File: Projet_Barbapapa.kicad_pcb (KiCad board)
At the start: 4 copper layers, 88.1 x 106.6 mm, 33 parts, among them J1 USB_C_Receptacle_USB2.0, J2 Speaker, J3 Conn_01x02, J4 LCD SPI, J5 LCD Soft SPI, J6 Random FTDI, J7 NFC1, J8 NFC2, J9 RGB_LED, SW1 SW_DPST, U1 MAX98357A/B, U2 AP61201Z6-7 buck, U3 MAX1811, U4 CD4051B

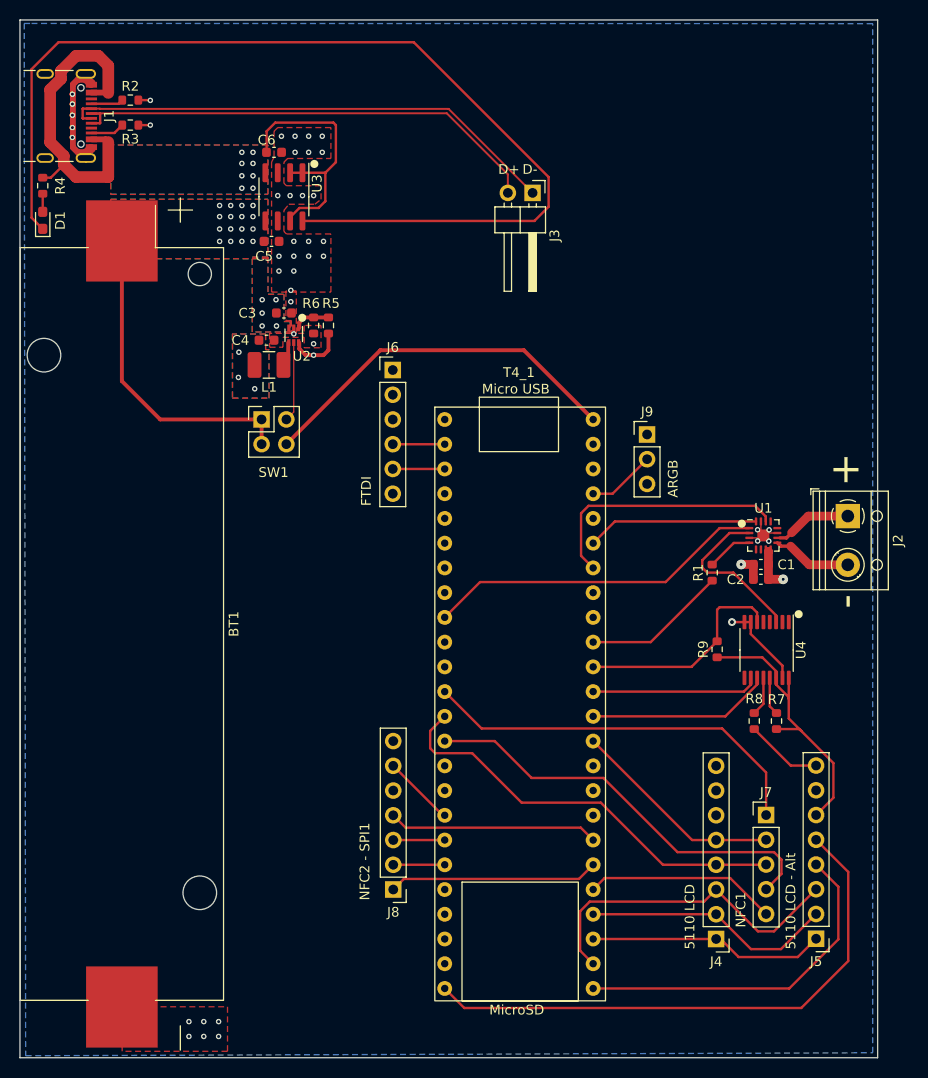
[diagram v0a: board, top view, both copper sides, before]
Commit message: Améliorations après retour Victor
Allumage du régulateur maintenant géré par la teensy
Compaction de la carte pour rentrer sur 100x100mm
Ajout des trous de montage
Routage de la puissance du port USB maintenant sans boucle !
Un peu plus d'espace pour l'ampli'
Routage de l'ampli' avec des plans sur la sortie et une via par
condo pour l'entrée.
Moins de vias thermiques
Un seule via dans le pad de l'ampli'
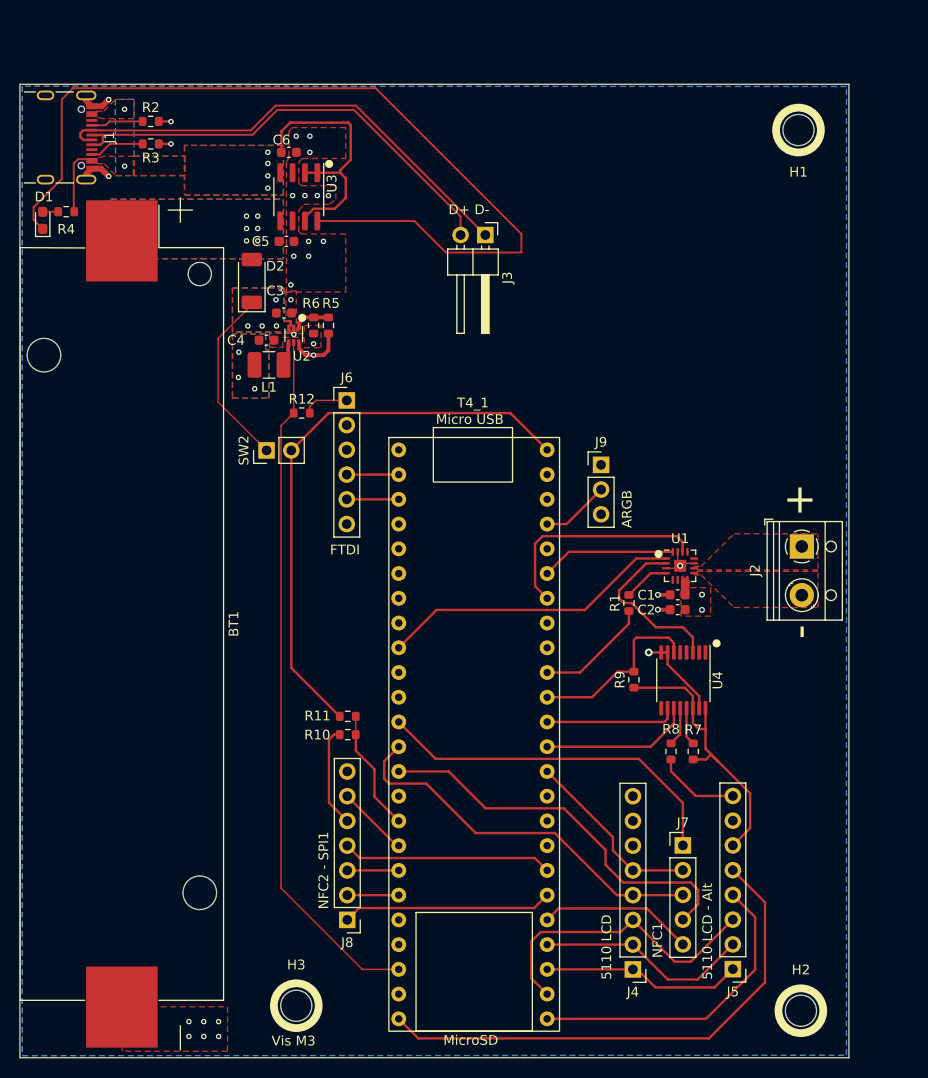
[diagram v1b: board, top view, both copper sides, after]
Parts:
- removed SW1: SW_DPST, Connector_PinHeader_2.54mm:PinHeader_2x02_P2.54mm_Vertical
- added D2: PMEG3050EP-QX, Diode_SMD:D_SOD-128, F.Cu at (41.4, 82.3)
- added H1: MountingHole, MountingHole:MountingHole_3.2mm_M3, F.Cu at (97.5, 66.8)
- added H2: MountingHole, MountingHole:MountingHole_3.2mm_M3, F.Cu at (97.8, 157.2)
- added H3: MountingHole, MountingHole:MountingHole_3.2mm_M3, F.Cu at (46.0, 156.7)
- added R10: RES_0603_200k_1%, 01_Passives:RES_0603, F.Cu at (51.3, 128.9)
- added R11: RES_0603_100K_1%, 01_Passives:RES_0603, F.Cu at (51.3, 127.0)
- added R12: RES_0603_5K1_1%, 01_Passives:RES_0603, F.Cu at (46.5, 95.9)
- added SW2: Power switch, Connector_PinHeader_2.54mm:PinHeader_1x02_P2.54mm_Vertical, F.Cu at (42.9, 99.7)
- R9: value RES_0603_2K1_1% -> RES_0603_5K1_1%
- moved J4 9.10 mm to (80.5, 153.0)
- moved C1 9.10 mm to (85.1, 114.5)
- moved C2 9.10 mm to (85.1, 116.0)
- moved J5 9.10 mm to (90.8, 153.0)
- moved J7 9.10 mm to (85.7, 140.3)
- moved R1 9.10 mm to (80.1, 115.4)
- moved R9 9.10 mm to (80.6, 123.2)
- moved U1 9.10 mm to (85.4, 111.5)
- moved U4 9.10 mm to (85.7, 123.3)
- moved R7 9.10 mm to (86.7, 130.6)
- moved R8 9.10 mm to (84.4, 130.6)
- moved J3 6.50 mm to (65.4, 77.6)
- moved J9 5.66 mm to (77.3, 101.2)
- moved J6 5.66 mm to (51.2, 94.6)
- moved J2 5.66 mm to (97.9, 109.6)
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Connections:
- C3 pad 1: /Power and USB/BATT_LOAD -> /Power and USB/BATT_SAFE
- T4_1 pad 24: unconnected-(T4_1-A10-Pad24) -> /BAT_SNS
- T4_1 pad 30: unconnected-(T4_1-Pad30) -> /Reg_en
- U2 pad 3: /Power and USB/BATT_LOAD -> /Power and USB/BATT_SAFE
- U2 pad 5: /Power and USB/Reg_en -> /Reg_en
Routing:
- net /Reg_en: track 0.00 -> 72.1 mm
- net /Power and USB/BATT_LOAD: track 32.9 -> 0.00 mm, vias 21 -> 6
- net /Power and USB/VBUS: track 60.7 -> 34.0 mm, vias 8 -> 6
- net /Power and USB/VIN: track 38.4 -> 58.8 mm
- net /Power and USB/BATT_SAFE: track 0.00 -> 18.8 mm, vias 0 -> 4
- net Net-(D1-K): track 105.8 -> 93.0 mm
- net /BAT_SNS: track 0.00 -> 12.6 mm
- net /Power and USB/Reg_en: track 8.21 -> 0.00 mm
- net /Audio/Speaker_N: track 8.17 -> 0.00 mm
- net /Audio/Speaker_P: track 7.88 -> 0.00 mm
- net /LCD connectors/LCD_SCK_ALT: track 58.1 -> 53.7 mm
- net /LCD connectors/LCD_RST: track 24.4 -> 20.2 mm
- net /LCD connectors/LCD_CS: track 25.9 -> 22.0 mm
- net /Audio_OUT: track 35.1 -> 31.2 mm
- net /NFC1_RST: track 19.8 -> 15.9 mm
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- added copper zone on F.Cu, net /Audio/Speaker_N
- added copper zone on F.Cu, net /Audio/Speaker_P
- added copper zone on B.Cu, net /Power and USB/BATT_SAFE
- added copper zone on F.Cu, net /Power and USB/BATT_SAFE
- added copper zone on In2.Cu, net /Power and USB/BATT_SAFE
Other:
- board size 88.1 x 106.6 mm -> 85.1 x 99.9 mm
- board text added: "L1 to the right One hop this time Bouger les résistances"
- board text added: "Vis M3"
- board text removed: "Pour dissipation thermique : ils disent de mettre des vias dans le pad, comment ?"
- board text removed: "The fuck do I do for thermal dissipation ? Ça dit de mettre des vias, mais pas de specs de dimension/nombre..."

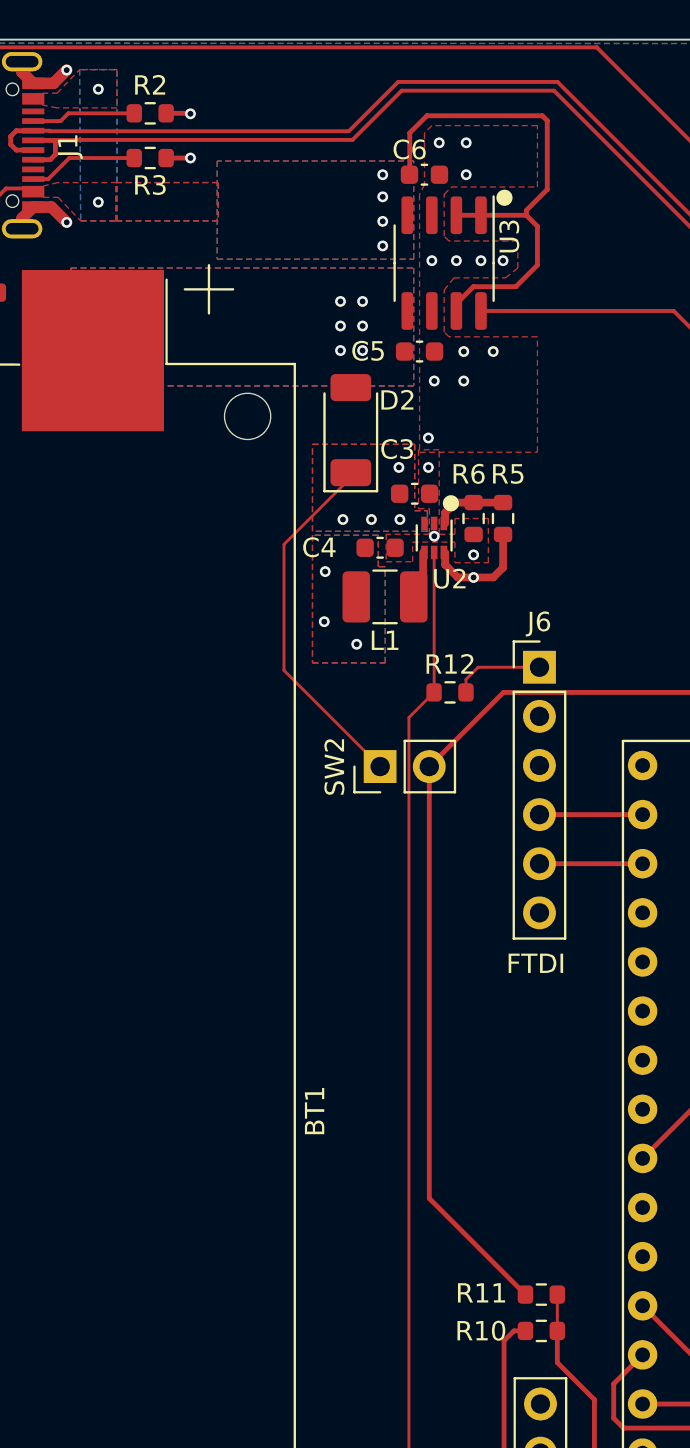
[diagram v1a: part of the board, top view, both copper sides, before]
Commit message: Inversion de la bobine de régulateur
180° à la bobine du régulateur pour faciliter le routage et le placement
Plus d'espace autour du régulateur.
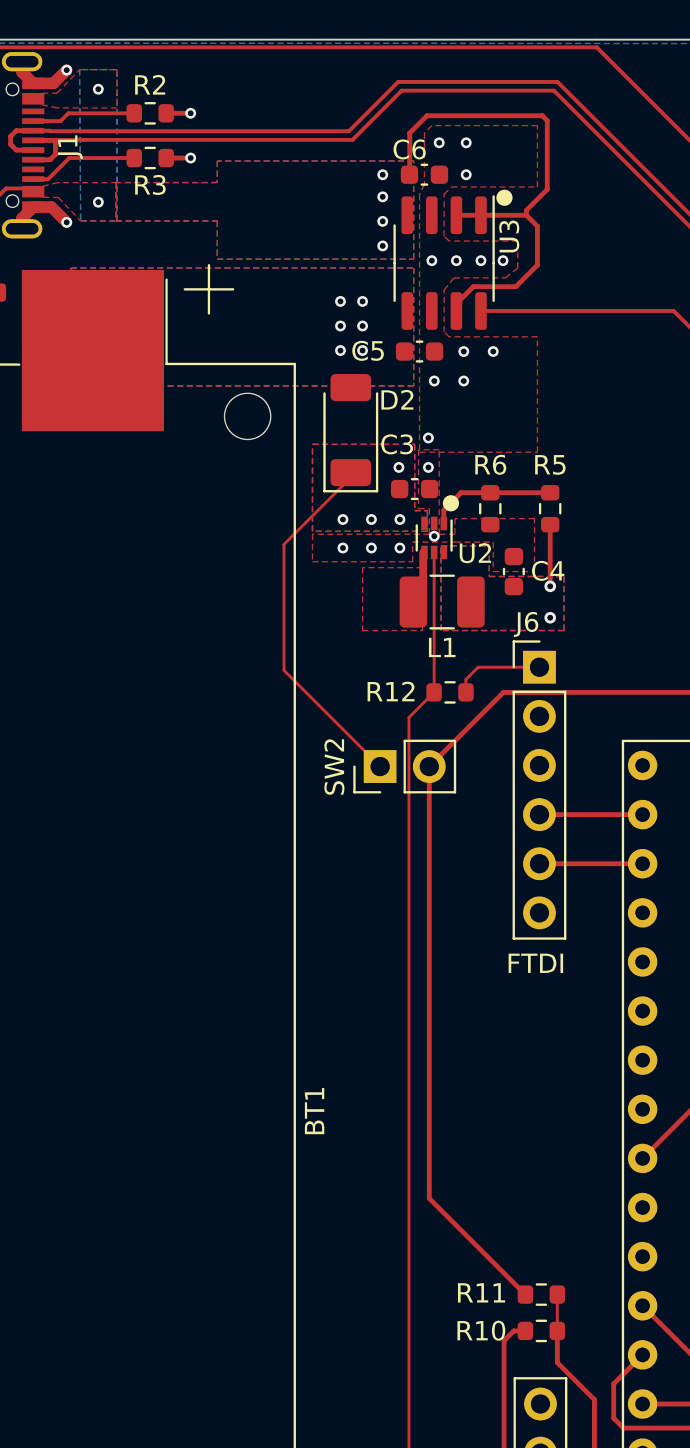
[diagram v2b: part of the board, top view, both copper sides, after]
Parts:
- moved C4 7.03 mm to (49.8, 89.6), turned to -90 degrees
- moved L1 2.97 mm to (46.1, 91.2), turned to 0 degrees
- moved R5 2.49 mm to (51.7, 86.4)
- moved R6 1.00 mm to (48.6, 86.4)
- moved C3 0.24 mm to (44.7, 85.3)
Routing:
- net Net-(U2-FB): track 3.77 -> 6.57 mm
- net /+3.3V: track 37.7 -> 35.0 mm, vias 6 -> 4
- net Net-(U2-SW): track 2.50 -> 1.82 mm
- net VSS: track 48.3 -> 48.2 mm, vias 29 -> 31
- added copper zone on F.Cu, net Net-(U2-SW)
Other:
- board text removed: "L1 to the right One hop this time Bouger les résistances"

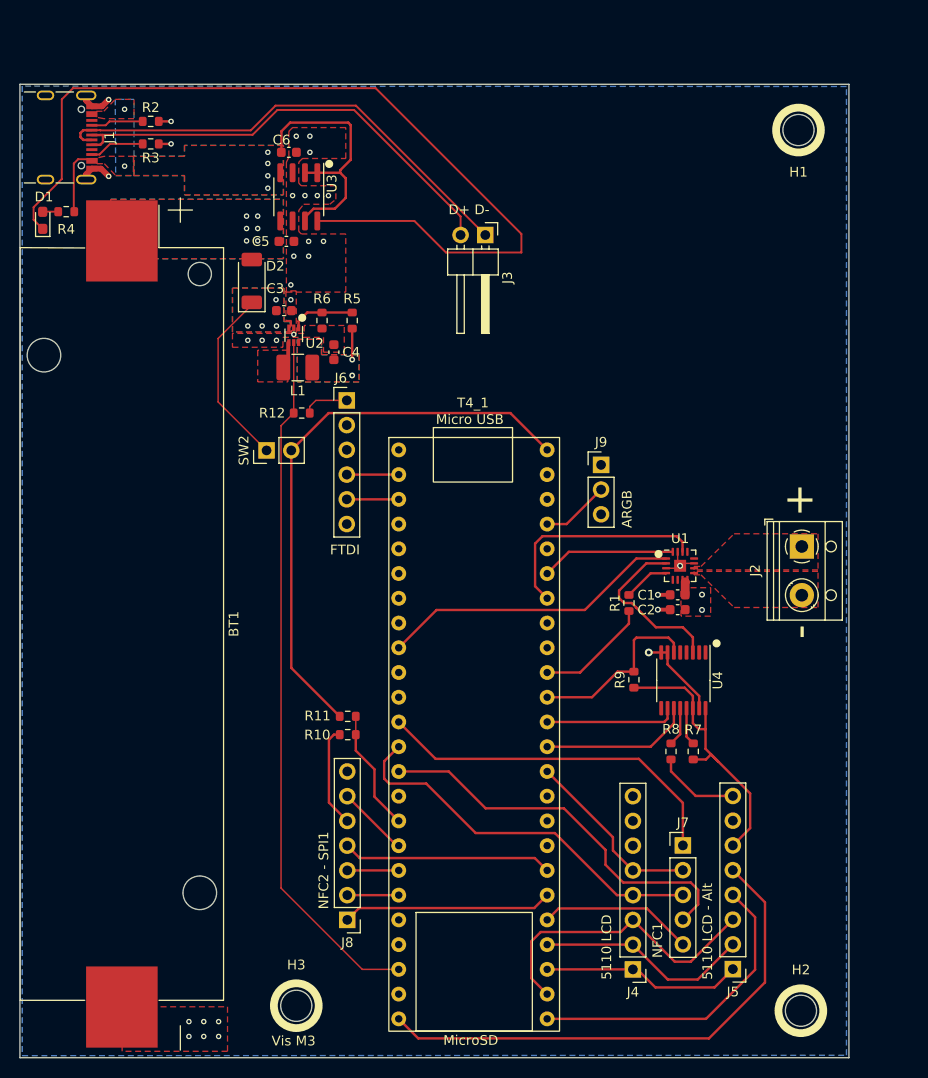
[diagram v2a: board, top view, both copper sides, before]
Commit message: Rev 0.3: Passage sur deux couches
Passage sur deux couches, ajustement de l'impédance pour l'USB.
Reroutage de l'alimentation côté USB
Ajout de beaucoup de silk
Quelques ajustements de nets pour la lisbilité
Ajout de LEDs de debug
Plan de masse sur le top
Quelques mises à jour sur le schematic
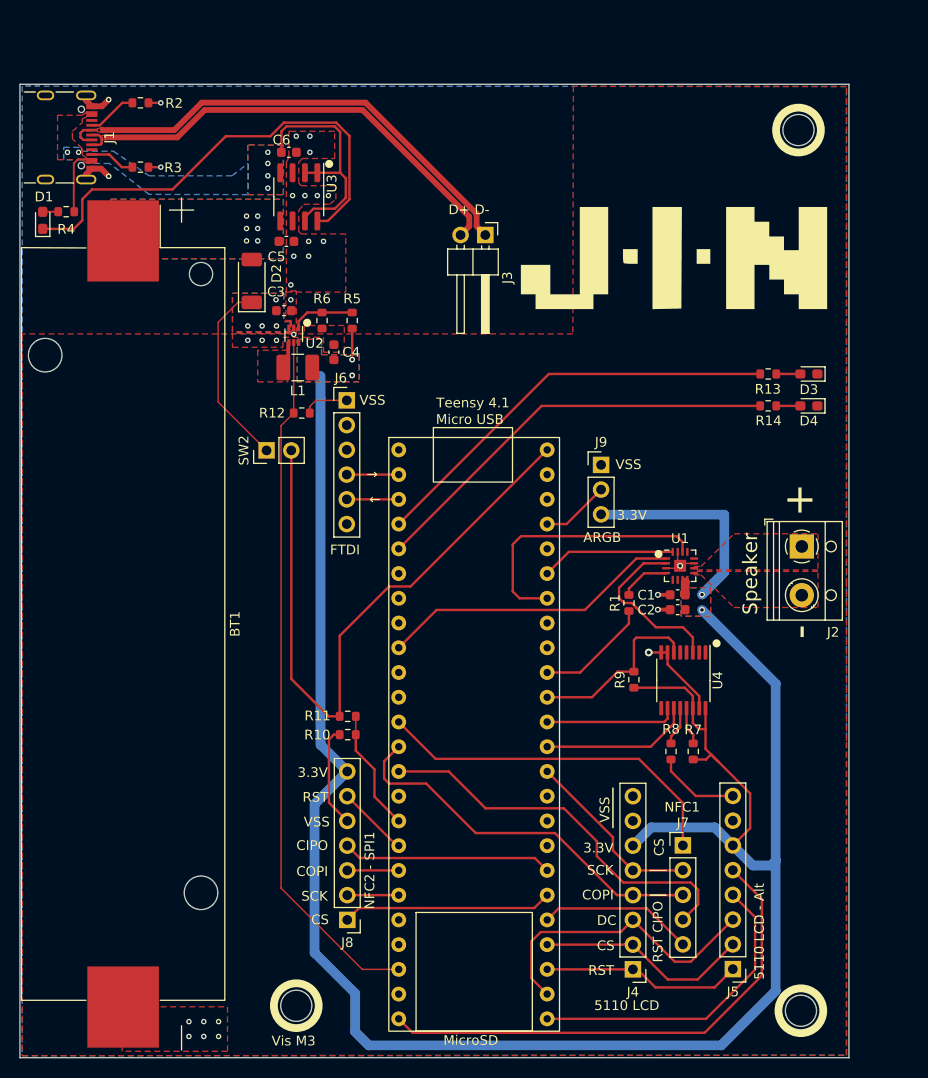
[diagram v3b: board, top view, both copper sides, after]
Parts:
- added D3: LED, LED_SMD:LED_0603_1608Metric_Pad1.05x0.95mm_HandSolder, F.Cu at (98.6, 91.8)
- added D4: LED, LED_SMD:LED_0603_1608Metric_Pad1.05x0.95mm_HandSolder, F.Cu at (98.6, 95.1)
- added G***: LOGO, LOGO, F.Cu at (85.2, 80.2)
- added G***: LOGO, LOGO, F.Cu at (80.9, 86.6)
- added R13: RES_0603_200_1%, 01_Passives:RES_0603, F.Cu at (94.4, 91.8)
- added R14: RES_0603_200_1%, 01_Passives:RES_0603, F.Cu at (94.4, 95.1)
- added REF**: OSHW-Logo2_14.6x12mm_SilkScreen, Symbol:OSHW-Logo2_14.6x12mm_SilkScreen, B.Cu at (28.0, 88.2)
- Teensy 4.1: renamed from T4_1
- moved R3 2.61 mm to (30.0, 70.6)
- moved R2 2.18 mm to (30.0, 64.0)
- moved BT1 0.13 mm to (28.2, 117.5)
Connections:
- net /+3.3V renamed VDD
- net Net-(J9-Pin_2) renamed /ARGB_Data
- Teensy 4.1 pad 2: unconnected-(T4_1-OUT2-Pad2) -> /DBG_LED_1
- Teensy 4.1 pad 3: unconnected-(T4_1-LRCLK2-Pad3) -> /DBG_LED_2
- Teensy 4.1 pad 59: unconnected-(T4_1-GND-Pad59) -> VSS
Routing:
- net VDD: track 35.0 -> 234.0 mm
- net Net-(D1-K): track 93.0 -> 48.6 mm
- net /DBG_LED_1: track 0.00 -> 43.5 mm
- net /DBG_LED_2: track 0.00 -> 43.2 mm
- net /Power and USB/VIN: track 58.8 -> 67.5 mm
- net /Audio/LRCLK: track 22.8 -> 27.7 mm
- net Net-(D3-A): track 0.00 -> 2.48 mm
- net Net-(D4-A): track 0.00 -> 2.47 mm
- net /Power and USB/VBUS: track 34.0 -> 31.7 mm
- net /LCD connectors/LCD_SCK_ALT: track 53.7 -> 52.4 mm
- net /Power and USB/BATT_SAFE: track 18.8 -> 19.8 mm
- net Net-(J1-CC2): track 5.67 -> 4.70 mm
- net /Power and USB/USB_D_P: track 48.5 -> 48.0 mm
- added copper zone on F.Cu, net /Power and USB/USB_D_N
- added copper zone on F.Cu, net /Power and USB/USB_D_P
- removed copper zone on In2.Cu, net /Power and USB/BATT_LOAD
- removed copper zone on In2.Cu, net /Power and USB/BATT_SAFE
- removed copper zone on In2.Cu, net VDD
- removed copper zone on In1.Cu, net VSS
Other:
- copper layers 4 -> 2
- board text added: "${TITLE} v${REVISION} Par ${COMPANY} Avec les conseils de : Victor Védie François Charles Lucas Molia"
- board text added: "3.3V"
- board text added: "CIPO"
- board text added: "COPI"
- board text added: "CS"
- board text added: "DC"
- board text added: "RST"
- board text added: "SCK"
- board text added: "Speaker"
- board text added: "VSS"
- board text added: "→"
